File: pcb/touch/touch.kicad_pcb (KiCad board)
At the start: 4 copper layers, 99.1 x 17.8 mm, 22 parts, among them J1 HEADER-1x05, Q1 BSS138, Q2 BSS138, SW1 ALARM, SW2 MENU, SW3 SET, U1 AT42QT1070, U2 LP2981

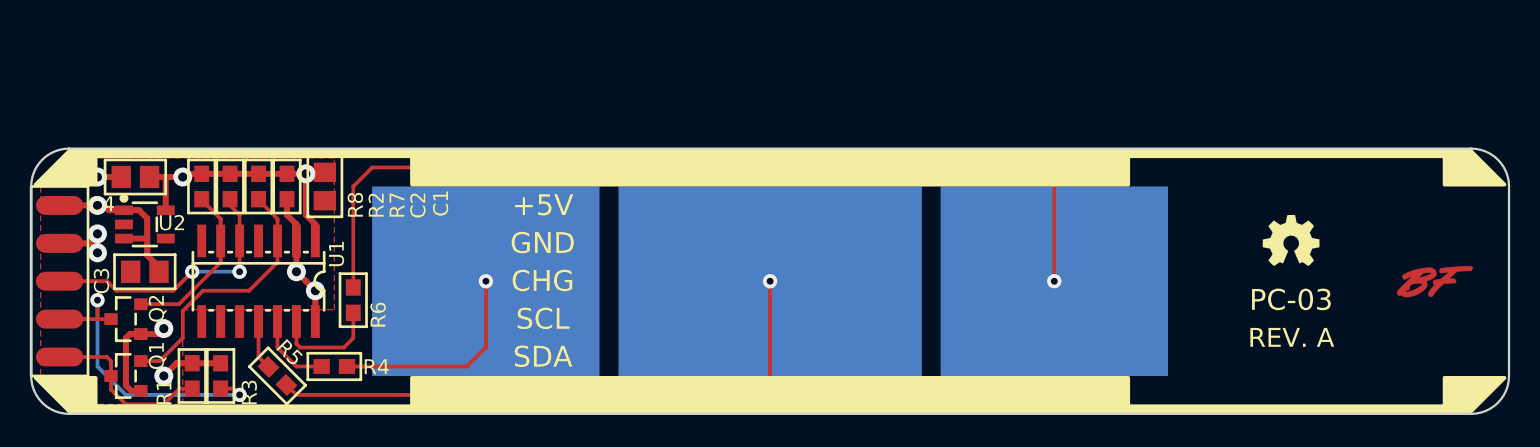
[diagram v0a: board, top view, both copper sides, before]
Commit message: Updated mechanical drawings, display panel. Rev B
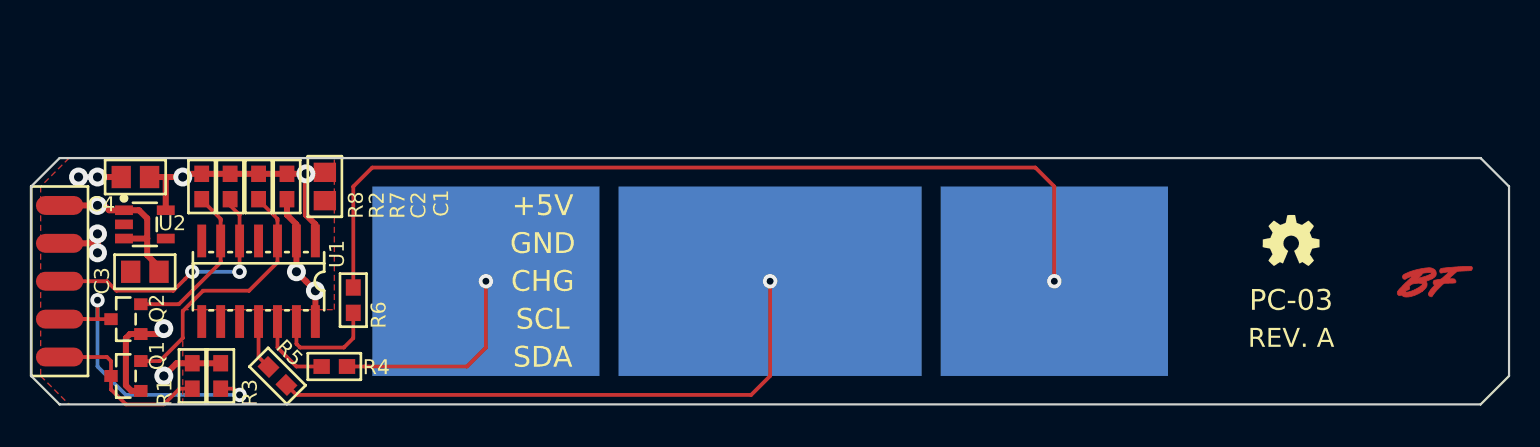
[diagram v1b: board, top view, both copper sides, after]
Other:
- board size 99.1 x 17.8 mm -> 99.1 x 16.5 mm
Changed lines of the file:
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@@
-(kicad_pcb (version 4) (host pcbnew "(2016-03-01 BZR 6238)-product")
+(kicad_pcb (version 4) (host pcbnew "(2016-05-03 BZR 6266)-product")
   (general
-    (links 0)
+    (links 37)
     (no_connects 0)
-    (area 98.984999 95.682999 198.195001 113.613001)
+    (area 98.715999 95.682999 198.195001 114.328319)
     (thickness 1.6)
     (drawings 15)
@@
       (xy 2.618853 -0.924247) (xy 2.624583 -0.881303) (xy 2.624583 -0.881303)) (layer F.Mask) (width 0.05))
   )
+  (gr_line (start 99.06 98.298) (end 100.965 96.393) (layer Edge.Cuts) (width 0.15))
+  (gr_line (start 198.12 98.298) (end 196.215 96.393) (layer Edge.Cuts) (width 0.15))
+  (gr_line (start 196.215 112.903) (end 198.12 110.998) (layer Edge.Cuts) (width 0.15))
+  (gr_line (start 99.06 110.998) (end 100.965 112.903) (layer Edge.Cuts) (width 0.15))
   (gr_text "REV. A" (at 183.515 108.458) (layer F.SilkS)
     (effects (font (size 1.27 1.27) (thickness 0.254)))
@@
     (effects (font (size 1.397 1.397) (thickness 0.3)))
   )
-  (gr_arc (start 101.6 110.998) (end 101.6 113.538) (angle 90) (layer Edge.Cuts) (width 0.15))
-  (gr_arc (start 101.6 98.298) (end 99.06 98.298) (angle 90) (layer Edge.Cuts) (width 0.15))
-  (gr_arc (start 195.58 98.298) (end 195.58 95.758) (angle 90) (layer Edge.Cuts) (width 0.15))
-  (gr_arc (start 195.58 110.998) (end 198.12 110.998) (angle 90) (layer Edge.Cuts) (width 0.15))
   (gr_line (start 99.06 98.298) (end 99.06 110.998) (angle 90) (layer Edge.Cuts) (width 0.15))
-  (gr_line (start 195.58 95.758) (end 101.6 95.758) (angle 90) (layer Edge.Cuts) (width 0.15))
+  (gr_line (start 196.215 96.393) (end 100.965 96.393) (angle 90) (layer Edge.Cuts) (width 0.15))
   (gr_line (start 198.12 110.998) (end 198.12 98.298) (angle 90) (layer Edge.Cuts) (width 0.15))
-  (gr_line (start 101.6 113.538) (end 195.58 113.538) (angle 90) (layer Edge.Cuts) (width 0.15))
+  (gr_line (start 100.965 112.903) (end 196.215 112.903) (angle 90) (layer Edge.Cuts) (width 0.15))
   (via (at 116.84 104.013) (size 1.27) (drill 0.6096) (layers F.Cu B.Cu) (net 1))
   (segment (start 103.505 97.663) (end 102.235 97.663) (width 0.4064) (layer B.Cu) (net 1))
@@
       )
     )
-  )
-  (zone (net 0) (net_name "") (layer F.SilkS) (hatch edge 0.508)
-    (connect_pads (clearance 0.4064))
-    (min_thickness 0.254)
-    (fill yes (arc_segments 16) (thermal_gap 0.508) (thermal_bridge_width 0.508))
-    (polygon
-      (pts
-        (xy 99.06 98.298) (xy 103.505 98.298) (xy 103.505 96.393) (xy 124.46 96.393) (xy 124.46 98.298)
-        (xy 172.72 98.298) (xy 172.72 96.393) (xy 193.675 96.393) (xy 193.675 98.298) (xy 198.12 98.298)
-        (xy 195.58 95.758) (xy 101.6 95.758)
-      )
-    )
-  )
-  (zone (net 0) (net_name "") (layer F.SilkS) (hatch edge 0.508)
-    (connect_pads (clearance 0.4064))
-    (min_thickness 0.254)
-    (fill yes (arc_segments 16) (thermal_gap 0.508) (thermal_bridge_width 0.508))
-    (polygon
-      (pts
-        (xy 198.12 110.998) (xy 193.675 110.998) (xy 193.675 112.903) (xy 172.72 112.903) (xy 172.72 110.998)
-        (xy 124.46 110.998) (xy 124.46 112.903) (xy 103.505 112.903) (xy 103.505 110.998) (xy 99.06 110.998)
-        (xy 101.6 113.538) (xy 195.58 113.538)
-      )
-    )

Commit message: Updated drawings - Display panel
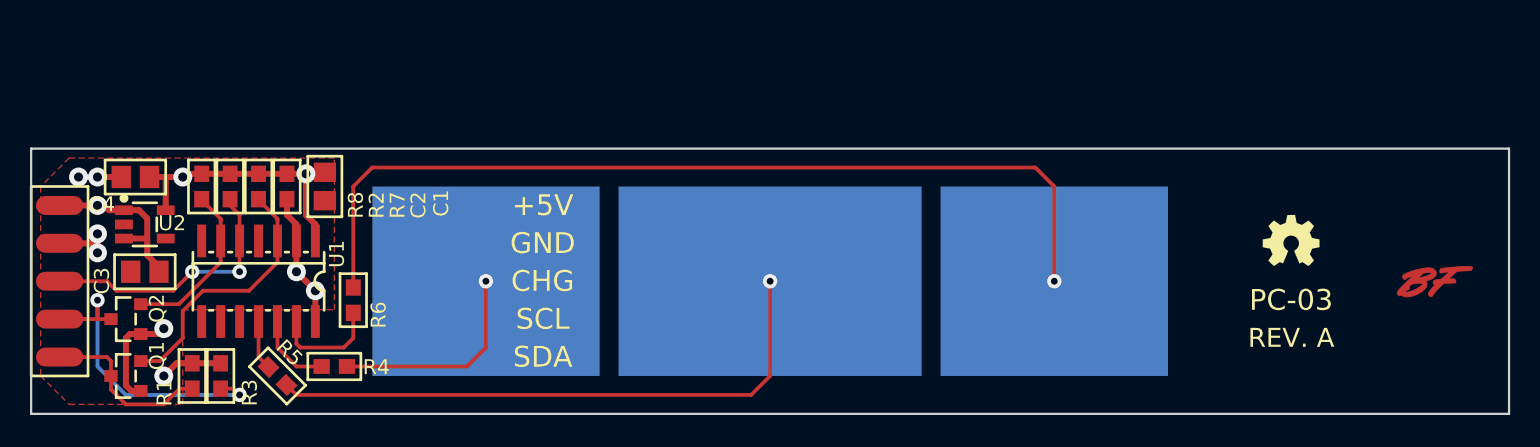
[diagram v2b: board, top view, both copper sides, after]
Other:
- board size 99.1 x 16.5 mm -> 99.1 x 17.8 mm
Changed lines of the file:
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@@
     (links 37)
     (no_connects 0)
-    (area 98.715999 95.682999 198.195001 114.328319)
+    (area 98.715999 95.734476 198.195001 114.328319)
     (thickness 1.6)
-    (drawings 15)
+    (drawings 11)
     (tracks 138)
     (zones 0)
@@
       (xy 2.618853 -0.924247) (xy 2.624583 -0.881303) (xy 2.624583 -0.881303)) (layer F.Mask) (width 0.05))
   )
-  (gr_line (start 99.06 98.298) (end 100.965 96.393) (layer Edge.Cuts) (width 0.15))
-  (gr_line (start 198.12 98.298) (end 196.215 96.393) (layer Edge.Cuts) (width 0.15))
-  (gr_line (start 196.215 112.903) (end 198.12 110.998) (layer Edge.Cuts) (width 0.15))
-  (gr_line (start 99.06 110.998) (end 100.965 112.903) (layer Edge.Cuts) (width 0.15))
   (gr_text "REV. A" (at 183.515 108.458) (layer F.SilkS)
     (effects (font (size 1.27 1.27) (thickness 0.254)))
@@
     (effects (font (size 1.397 1.397) (thickness 0.3)))
   )
-  (gr_line (start 99.06 98.298) (end 99.06 110.998) (angle 90) (layer Edge.Cuts) (width 0.15))
-  (gr_line (start 196.215 96.393) (end 100.965 96.393) (angle 90) (layer Edge.Cuts) (width 0.15))
-  (gr_line (start 198.12 110.998) (end 198.12 98.298) (angle 90) (layer Edge.Cuts) (width 0.15))
-  (gr_line (start 100.965 112.903) (end 196.215 112.903) (angle 90) (layer Edge.Cuts) (width 0.15))
+  (gr_line (start 99.06 95.758) (end 99.06 113.538) (angle 90) (layer Edge.Cuts) (width 0.15))
+  (gr_line (start 198.12 95.758) (end 99.06 95.758) (angle 90) (layer Edge.Cuts) (width 0.15))
+  (gr_line (start 198.12 113.538) (end 198.12 95.758) (angle 90) (layer Edge.Cuts) (width 0.15))
+  (gr_line (start 99.06 113.538) (end 198.12 113.538) (angle 90) (layer Edge.Cuts) (width 0.15))
   (via (at 116.84 104.013) (size 1.27) (drill 0.6096) (layers F.Cu B.Cu) (net 1))
   (segment (start 103.505 97.663) (end 102.235 97.663) (width 0.4064) (layer B.Cu) (net 1))

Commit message: Modified display panel frame, touch panel pcb
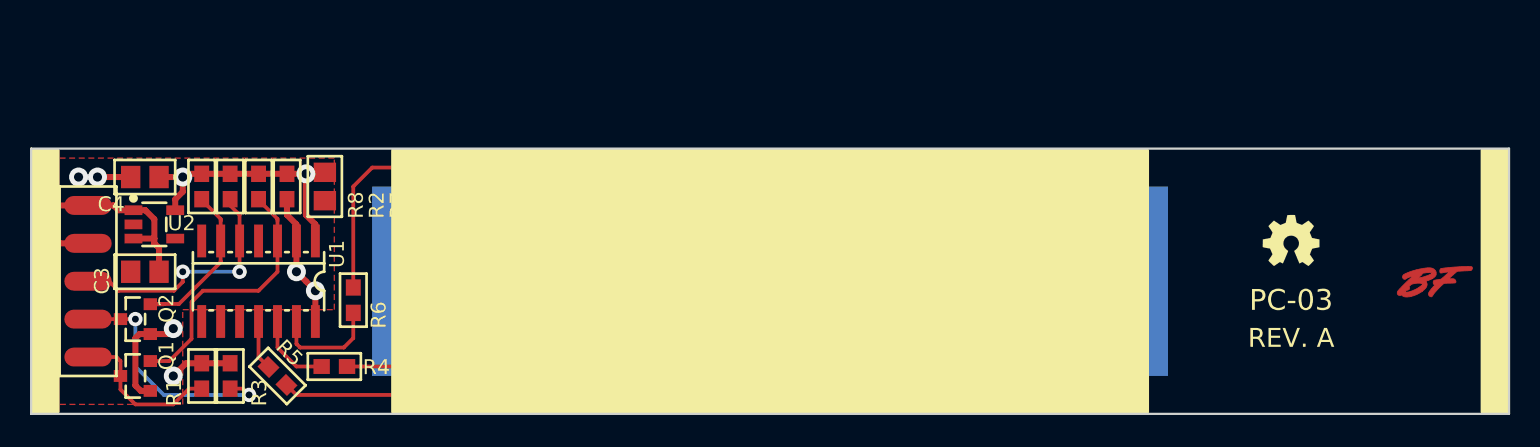
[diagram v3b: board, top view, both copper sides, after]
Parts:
- moved J1 1.91 mm to (102.9, 104.6)
- moved C4 0.64 mm to (106.7, 97.7)
- moved Q1 0.64 mm to (106.0, 111.0)
- moved Q2 0.64 mm to (106.0, 107.2)
- moved R1 0.63 mm to (110.5, 111.0)
- moved R3 0.63 mm to (112.4, 111.0)
- moved U2 0.63 mm to (107.3, 100.8)
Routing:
- net /SCL_5V: track 20.9 -> 17.5 mm
- net /SDA_5V: track 11.1 -> 13.0 mm
- net +5V: track 15.9 -> 17.1 mm
- net /~CHANGE: track 17.3 -> 16.5 mm

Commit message: * Fix wrong footprint for resistors (C-* to R-*) * Changed schematic sheet size to US letter
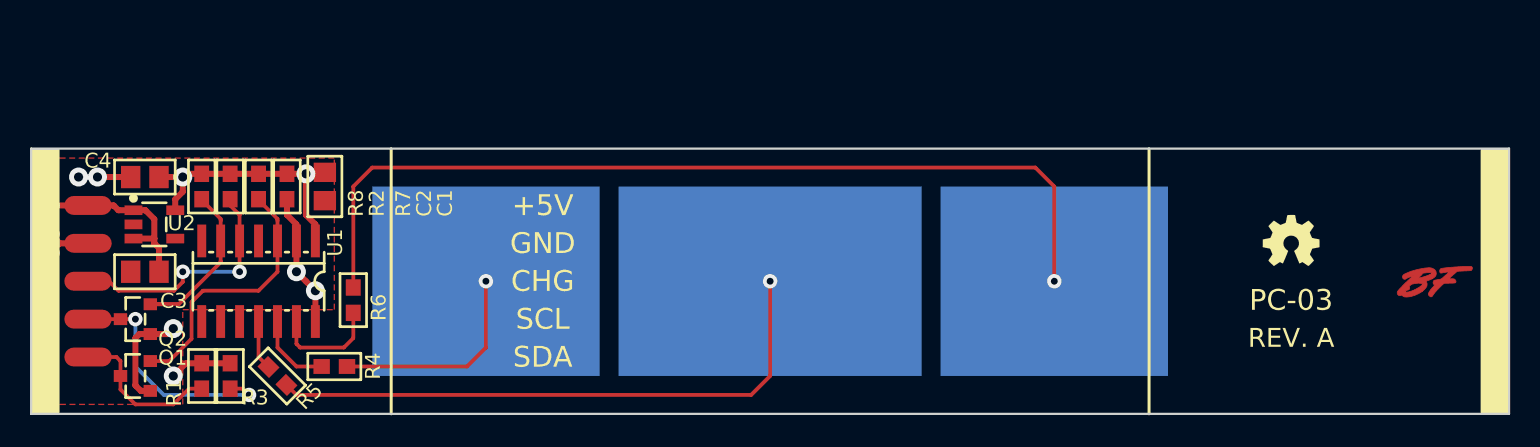
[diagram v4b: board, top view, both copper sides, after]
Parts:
- added REF**: VAL**, Symbols:Gauge-XY-100mm, F.Cu at (72.4, 142.7)
- R1, R2, R3, R4, R5, R6, R7, R8: footprint SMT:C-0603 -> SMT:R-0603
- SW1, SW2: footprint Conn-Wire-Pads:touchpad-600x500 -> Conn-Wire-Pads:TouchPad-600x500
- SW3: footprint Conn-Wire-Pads:touchpad-800x500 -> Conn-Wire-Pads:TouchPad-800x500
- U1: footprint SMT-SOIC:14N -> SMT-SOIC:SOIC14N

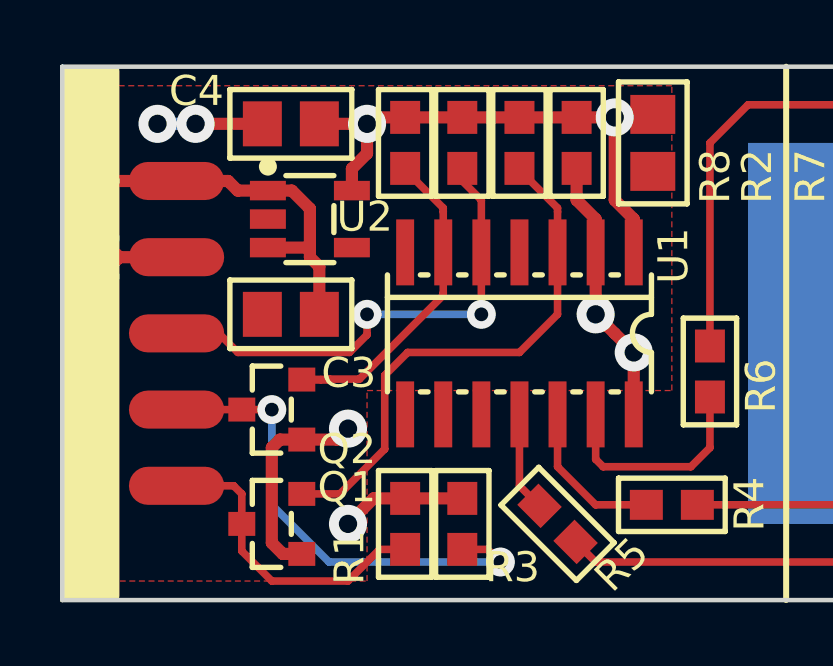
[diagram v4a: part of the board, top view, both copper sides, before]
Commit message: Changed touch keypad, front panel and light sensor pcb to a two layer design.
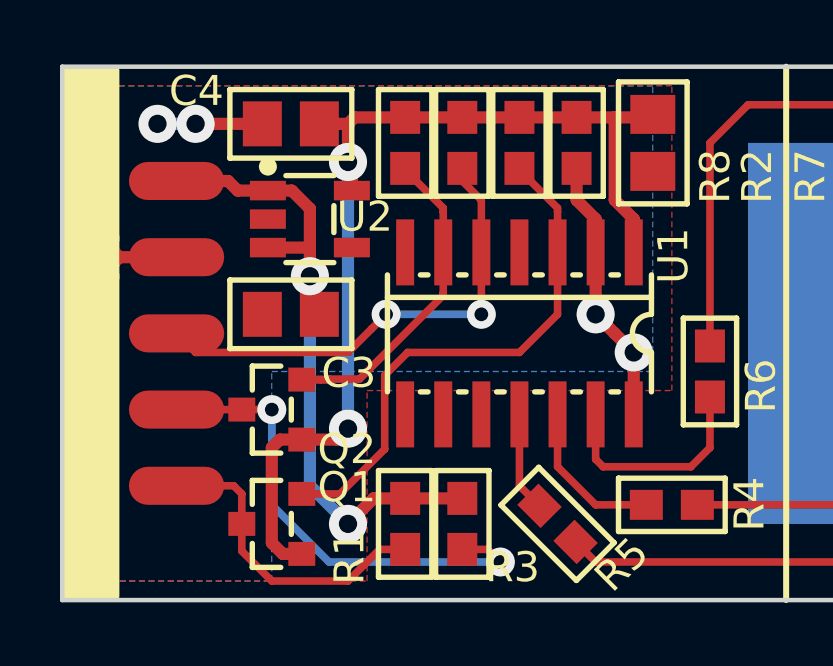
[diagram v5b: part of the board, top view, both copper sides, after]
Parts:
- removed the REF** at (72.4, 142.7)
- added REF**: VAL**, Symbols:Gauge-X-100mm, B.Cu at (92.7, 113.5)
- added REF**: VAL**, Symbols:Gauge-X-100mm, F.Cu at (99.1, 119.9)
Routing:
- net +3V3: track 26.0 -> 34.8 mm, vias 3 -> 2
- net +5V: track 17.1 -> 23.3 mm
- added copper zone on B.Cu, net GND
- removed copper zone on Power, net +3V3
- removed copper zone on Power, net +5V
- removed copper zone on GND, net GND
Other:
- copper layers 4 -> 2

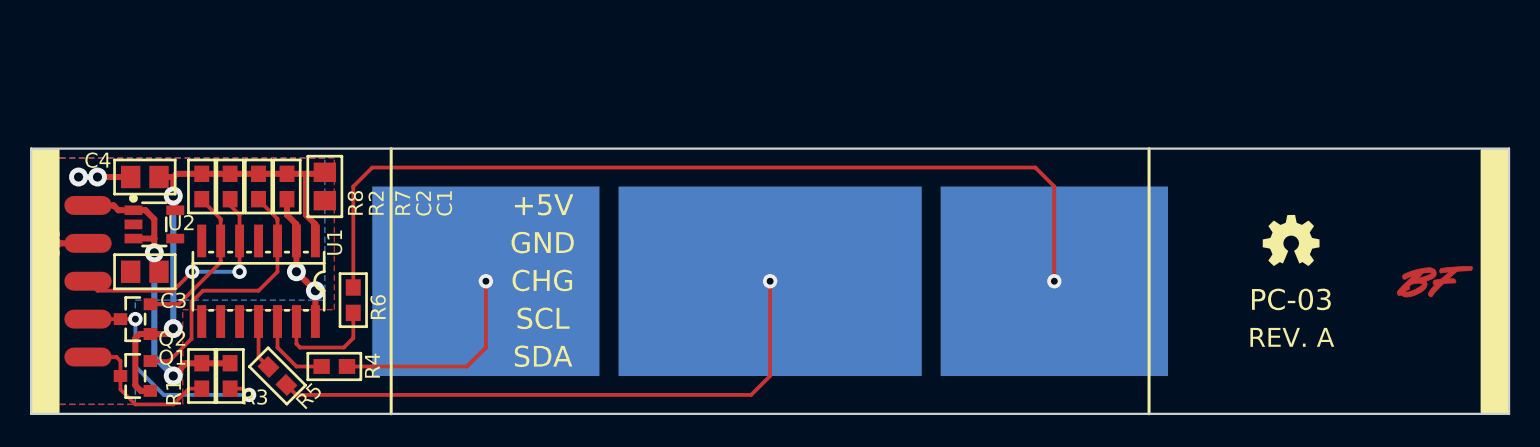
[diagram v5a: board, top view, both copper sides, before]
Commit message: Revised touch and front panel PCB, Added Motherboard PCB
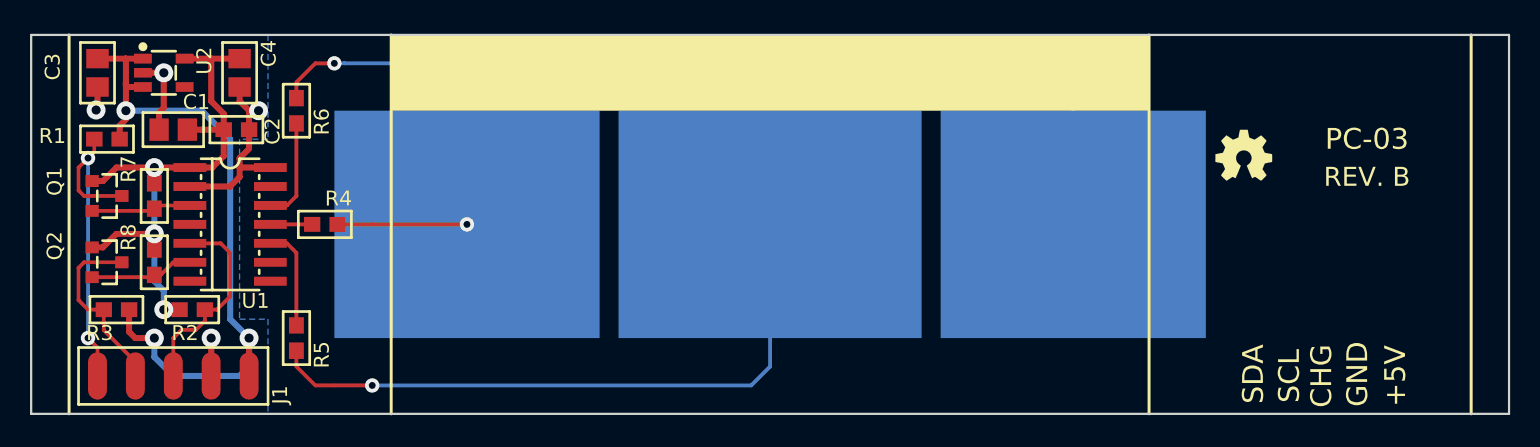
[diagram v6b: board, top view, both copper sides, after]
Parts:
- removed LOGO-OSHW-150: OSHW, Symbols:LOGO-OSHW-150
- removed the REF** at (92.7, 113.5)
- removed the REF** at (99.1, 119.9)
- removed SIGNATURE: LOGO, Symbols:SIGNATURE
- added REF**: VAL**, symbols:LOGO-OSHW-150, F.Cu at (180.3, 96.4)
- C1, C3, C4: footprint SMT:C-0805 -> smt:C-0805
- C2: footprint SMT:C-0603 -> smt:C-0603
- J1: footprint Conn-Wire-Pads:WP-50mil-1x05 -> conn-wire-pads:WP-50mil-1x05
- Q1, Q2: footprint SMT-SOT:SOT23 -> smt-sot:SOT23
- R1, R2, R3, R4, R5, R6, R7, R8: footprint SMT:R-0603 -> smt:R-0603
- SW1, SW2: footprint Conn-Wire-Pads:TouchPad-600x500 -> conn-wire-pads:TouchPad-700x600
- SW3: footprint Conn-Wire-Pads:TouchPad-800x500 -> conn-wire-pads:TouchPad-800x600
- U1: footprint SMT-SOIC:SOIC14N -> smt-soic:SOIC14N
- U2: value LP2981 -> LP2981-33DBVT; footprint SMT-SOT:SOT23-5 -> smt-sot:SOT23-5
- moved R1 17.1 mm to (104.1, 95.1), turned to 0 degrees
- moved C3 13.7 mm to (103.5, 90.7), turned to 90 degrees
- moved R6 13.3 mm to (116.8, 93.2)
- moved Q1 12.2 mm to (104.1, 98.9), turned to 270 degrees
- moved C1 10.9 mm to (108.6, 94.5), turned to 180 degrees
- moved U2 10.2 mm to (108.0, 90.7)
- moved R4 9.55 mm to (118.7, 100.8)
- moved C4 9.44 mm to (113.0, 90.7), turned to 90 degrees
- moved R3 8.82 mm to (104.8, 106.6), turned to 0 degrees
- moved R2 8.64 mm to (109.9, 106.6), turned to 0 degrees
- moved J1 8.54 mm to (108.6, 111.0), turned to 0 degrees
- moved R7 7.01 mm to (107.3, 98.9)
- moved R8 5.99 mm to (107.3, 103.4)
- moved C2 5.10 mm to (112.8, 94.5), turned to 0 degrees
- moved Q2 4.26 mm to (104.1, 103.4), turned to 270 degrees
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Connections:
- R4 pad 2: /E_LEFT -> /E_RIGHT
- R6 pad 2: /E_RIGHT -> /E_LEFT
- SW1 pad 1: /E_RIGHT -> /E_LEFT
- SW2 pad 1: /E_LEFT -> /E_RIGHT
- U1 pad 10: Net-(U1-Pad10) -> Net-(R5-Pad1)
- U1 pad 11: Net-(R5-Pad1) -> Net-(R4-Pad1)
- U1 pad 12: Net-(R4-Pad1) -> Net-(R6-Pad1)
- U1 pad 13: Net-(R6-Pad1) -> Net-(U1-Pad13)
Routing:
- net /E_RIGHT: track 61.2 -> 8.67 mm
- net /E_LEFT: track 14.3 -> 63.7 mm
- net +5V: track 23.3 -> 47.9 mm, vias 2 -> 3
- net /SDA_3V3: track 17.8 -> 6.71 mm
- net /SDA_5V: track 13.0 -> 21.8 mm, vias 0 -> 2
- net +3V3: track 34.8 -> 40.8 mm, vias 2 -> 3
- net GND: track 16.2 -> 21.7 mm, vias 6 -> 4
- net /SCL_5V: track 17.5 -> 12.5 mm, vias 2 -> 0
- net /SCL_3V3: track 11.5 -> 6.97 mm
- net /E_SET: track 39.6 -> 43.4 mm
- net Net-(R5-Pad1): track 3.33 -> 6.87 mm
- net /~CHANGE: track 16.1 -> 13.8 mm, vias 2 -> 0
- net Net-(R4-Pad1): track 4.60 -> 2.80 mm
- removed copper zone on F.Cu, net GND
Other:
- board size 99.1 x 17.8 mm -> 99.1 x 25.4 mm
- board text added: "ALARM - NEXT"
- board text added: "MENU - EXIT"
- board text added: "REV. B"
- board text added: "SET"
- board text removed: "REV. A"
